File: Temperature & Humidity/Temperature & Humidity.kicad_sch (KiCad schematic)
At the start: 19 parts, among them U1 ESP32-C3-MINI-1, U2 SHT4x, U3 MIC5504-3.3YM5

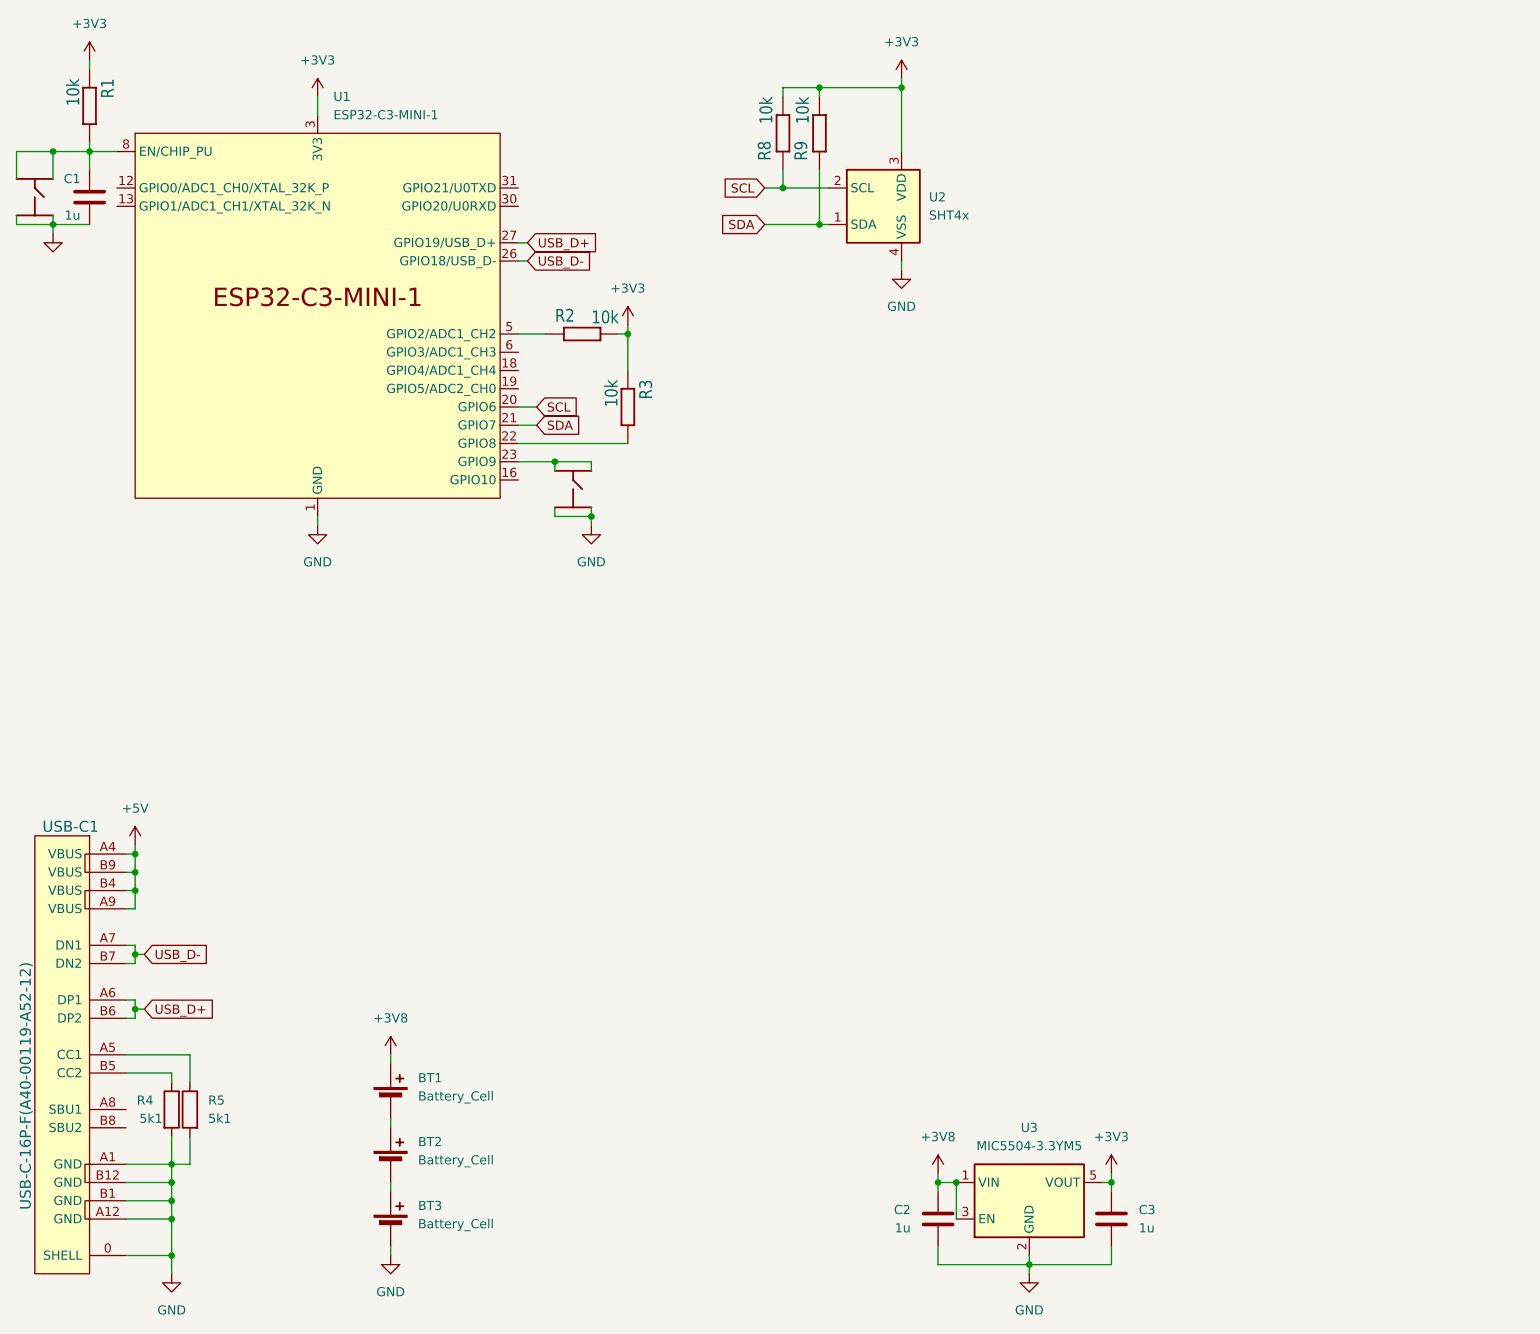
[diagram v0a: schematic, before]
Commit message: added battery level sensor
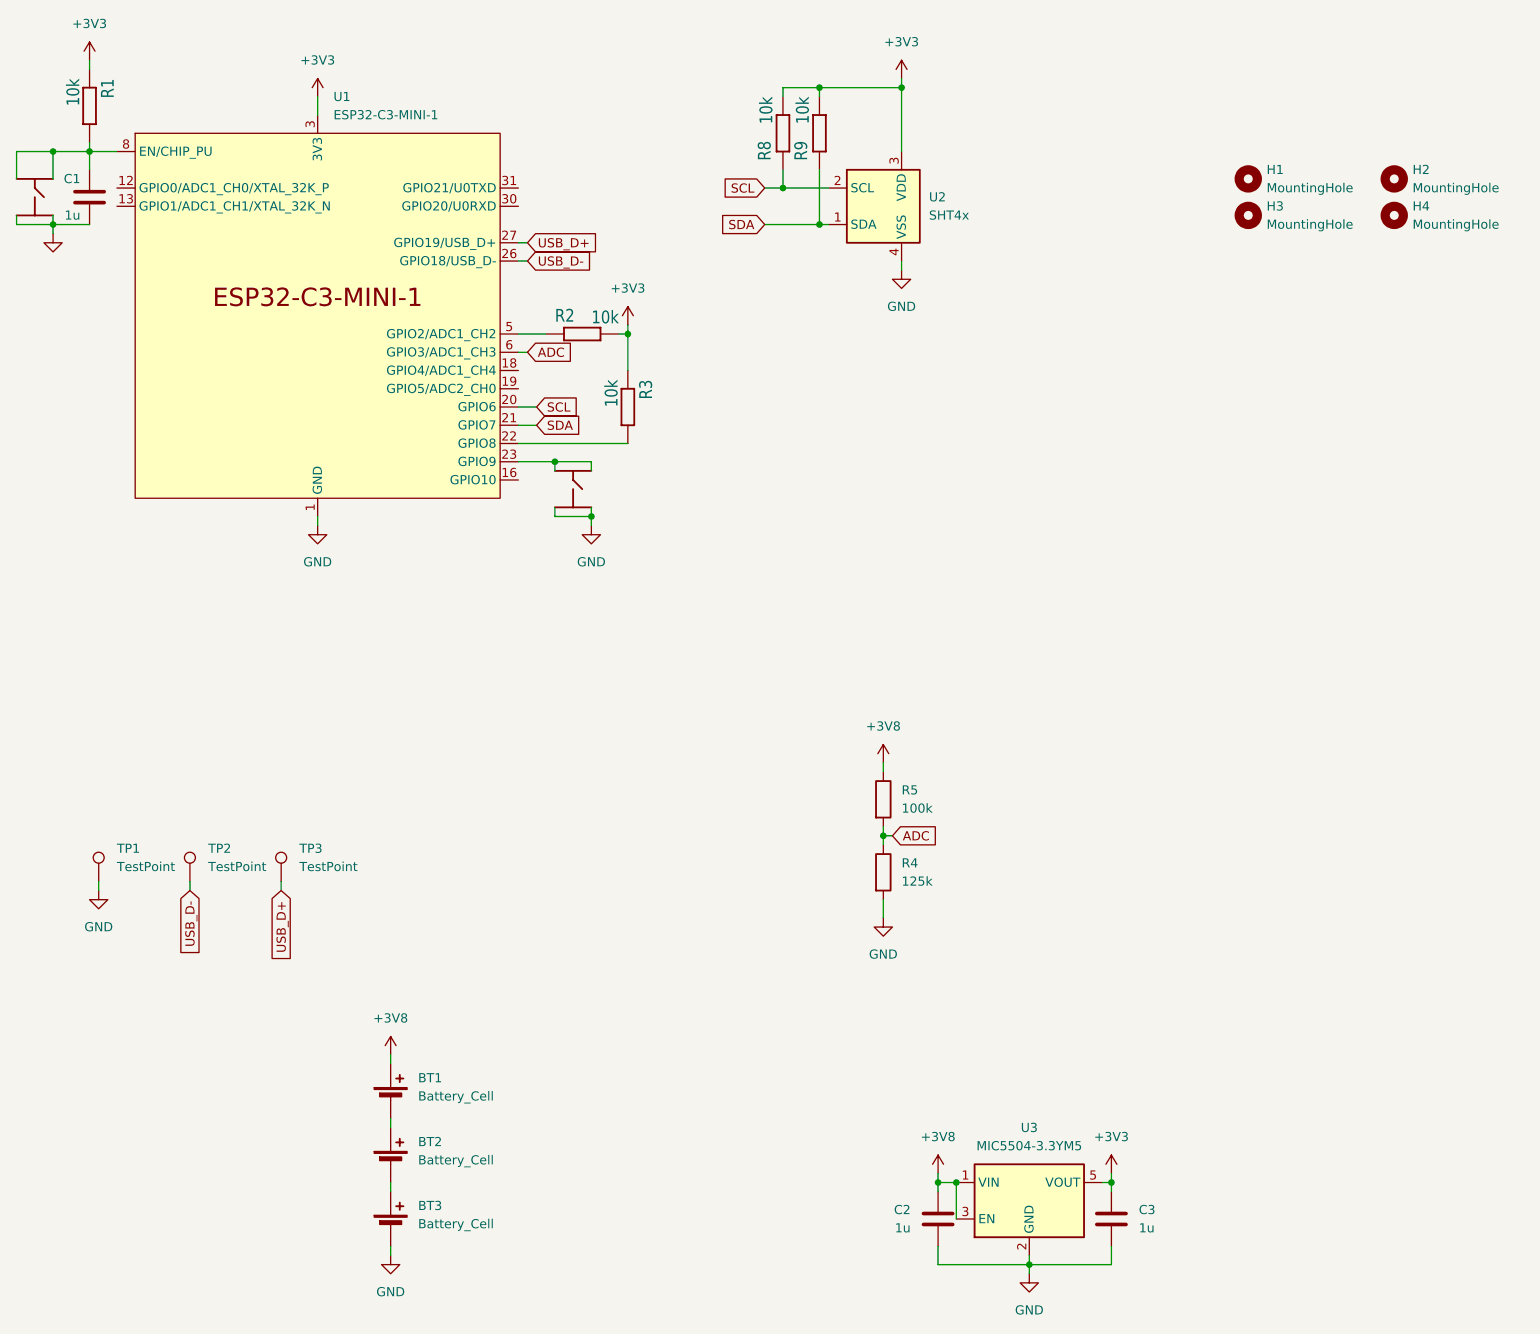
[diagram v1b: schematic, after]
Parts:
- removed USB-C1: USB-C-16P-F(A40-00119-A52-12), Personal:USB2.0_TYPE-C(A40-00119-A52-12), symbol personal2:USB2.0_TYPE-C(A40-00119-A52-12)
- added H1, H2, H3, H4: MountingHole, MountingHole:MountingHole_3.2mm_M3_DIN965_Pad, symbol Mechanical:MountingHole
- added TP1, TP2, TP3: TestPoint, TestPoint:TestPoint_Pad_D1.5mm, symbol Connector:TestPoint
- R4: value 5k1 -> 125k
- R5: value 5k1 -> 100k
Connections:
- net +3V8: now also R5.1
- net GND: now also TP1.1; no longer R5.2
- net USB_D+: now also TP3.1
- net USB_D-: now also TP2.1
- net ADC: now reaches U1.6 (GPIO3/ADC1_CH3)
- net ADC: now also R4.1, R5.2
